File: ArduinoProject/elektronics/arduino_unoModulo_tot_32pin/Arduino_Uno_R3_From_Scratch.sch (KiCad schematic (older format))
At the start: 0 parts

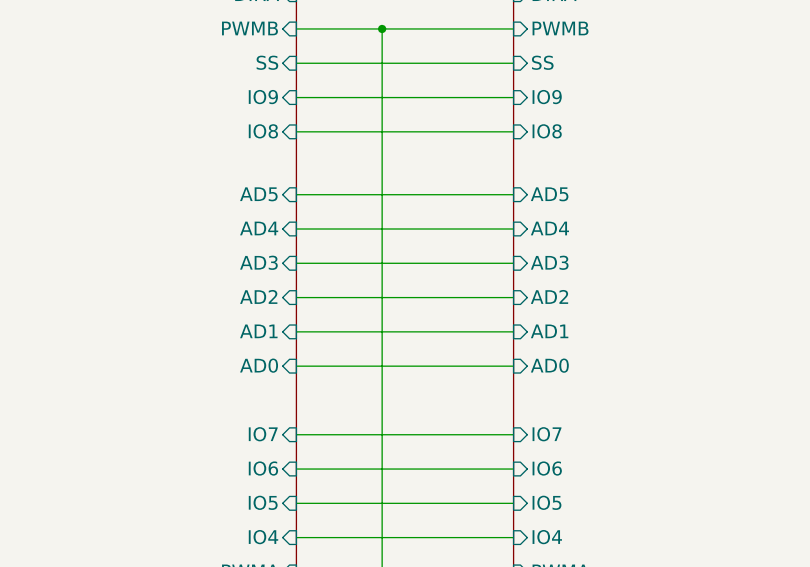
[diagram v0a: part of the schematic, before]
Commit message: analog pins added
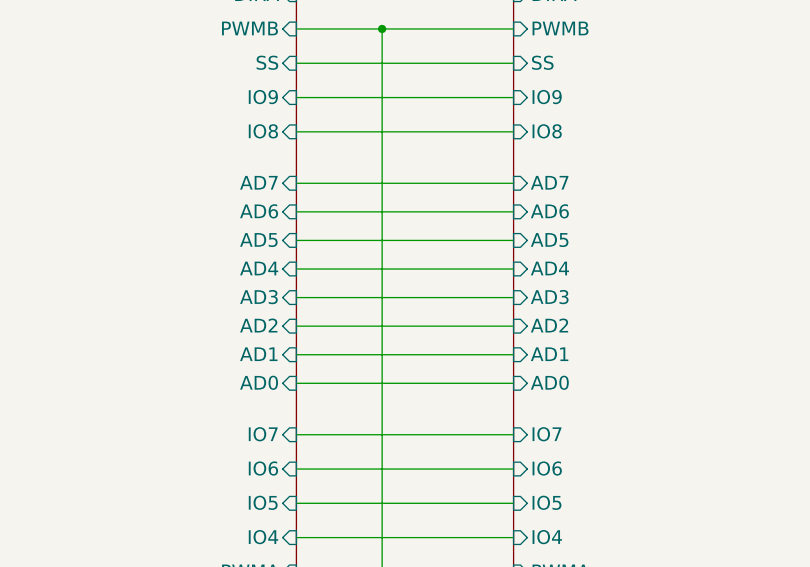
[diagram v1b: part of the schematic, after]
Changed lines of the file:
@@
 F0 "Headers" 50
 F1 "Headers.sch" 50
-F2 "AD3" I L 7875 2925 60
-F3 "AD2" I L 7875 3075 60
-F4 "AD1" I L 7875 3225 60
-F5 "AD0" I L 7875 3375 60
+F2 "AD3" I L 7875 3075 60
+F3 "AD2" I L 7875 3200 60
+F4 "AD1" I L 7875 3325 60
+F5 "AD0" I L 7875 3450 60
 F6 "IO7" I L 7875 3675 60
 F7 "IO6" I L 7875 3825 60
@@
 F22 "RESET" I L 7875 1225 60
 F23 "VIN" I R 9375 4550 60
-F24 "AD5" I L 7875 2625 60
-F25 "AD4" I L 7875 2775 60
+F24 "AD5" I L 7875 2825 60
+F25 "AD4" I L 7875 2950 60
+F26 "AD7" I L 7875 2575 60
+F27 "AD6" I L 7875 2700 60
 $EndSheet
 $Sheet
@@
 F1 "ATMEGA328P.sch" 50
 F2 "AREF" I R 6925 1075 60
-F3 "AD5" I R 6925 2625 60
-F4 "AD4" I R 6925 2775 60
-F5 "AD3" I R 6925 2925 60
-F6 "AD2" I R 6925 3075 60
-F7 "AD1" I R 6925 3225 60
-F8 "AD0" I R 6925 3375 60
+F3 "AD5" I R 6925 2825 60
+F4 "AD4" I R 6925 2950 60
+F5 "AD3" I R 6925 3075 60
+F6 "AD2" I R 6925 3200 60
+F7 "AD1" I R 6925 3325 60
+F8 "AD0" I R 6925 3450 60
 F9 "IO7" I R 6925 3675 60
 F10 "IO6" I R 6925 3825 60
@@
 F22 "DIRB" I R 6925 1600 60
 F23 "RESET" I R 6925 1225 60
+F24 "AD6" I R 6925 2700 60
+F25 "AD7" I R 6925 2575 60
 $EndSheet
 Wire Wire Line
@@
 Wire Wire Line
 	6925 2350 7875 2350
-Wire Wire Line
-	6925 2625 7875 2625
-Wire Wire Line
-	6925 2775 7875 2775
-Wire Wire Line
-	6925 2925 7875 2925
-Wire Wire Line
-	6925 3075 7875 3075
-Wire Wire Line
-	6925 3225 7875 3225
-Wire Wire Line
-	6925 3375 7875 3375
 Wire Wire Line
 	6925 3675 7875 3675
@@
 	7275 575  7275 1600
 Connection ~ 7275 1600
+Wire Wire Line
+	7875 3450 6925 3450
+Wire Wire Line
+	6925 3325 7875 3325
+Wire Wire Line
+	6925 3200 7875 3200
+Wire Wire Line
+	6925 3075 7875 3075
+Wire Wire Line
+	6925 2950 7875 2950
+Wire Wire Line
+	6925 2825 7875 2825
+Wire Wire Line
+	6925 2575 7875 2575
+Wire Wire Line
+	6925 2700 7875 2700
 $EndSCHEMATC

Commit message: arduino routint altered2
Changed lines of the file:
@@
 F2 "OUT1" I R 2650 3225 60
 F3 "OUT2" I R 2650 3325 60
-F4 "OUT4" I R 2650 3425 60
-F5 "OUT3" I R 2650 3525 60
+F4 "OUT4" I R 2650 3525 60
+F5 "OUT3" I R 2650 3425 60
 F6 "PWRIN" I L 1200 3275 60
 $EndSheet
